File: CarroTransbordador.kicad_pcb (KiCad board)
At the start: 2 copper layers, 172.4 x 87.6 mm, 36 parts, among them J10 VIN- Pin, J11 VOUT+ Pin, J12 VOUT- Pin, J13 Borner ESP32, J14 Conn. Conv. HV, J15 Conn. Conv. LV, J16 Conn. ESP32, J17 Conn. LED Tr., J18 Conn. LED Empot., J19 Conn. LED Polea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

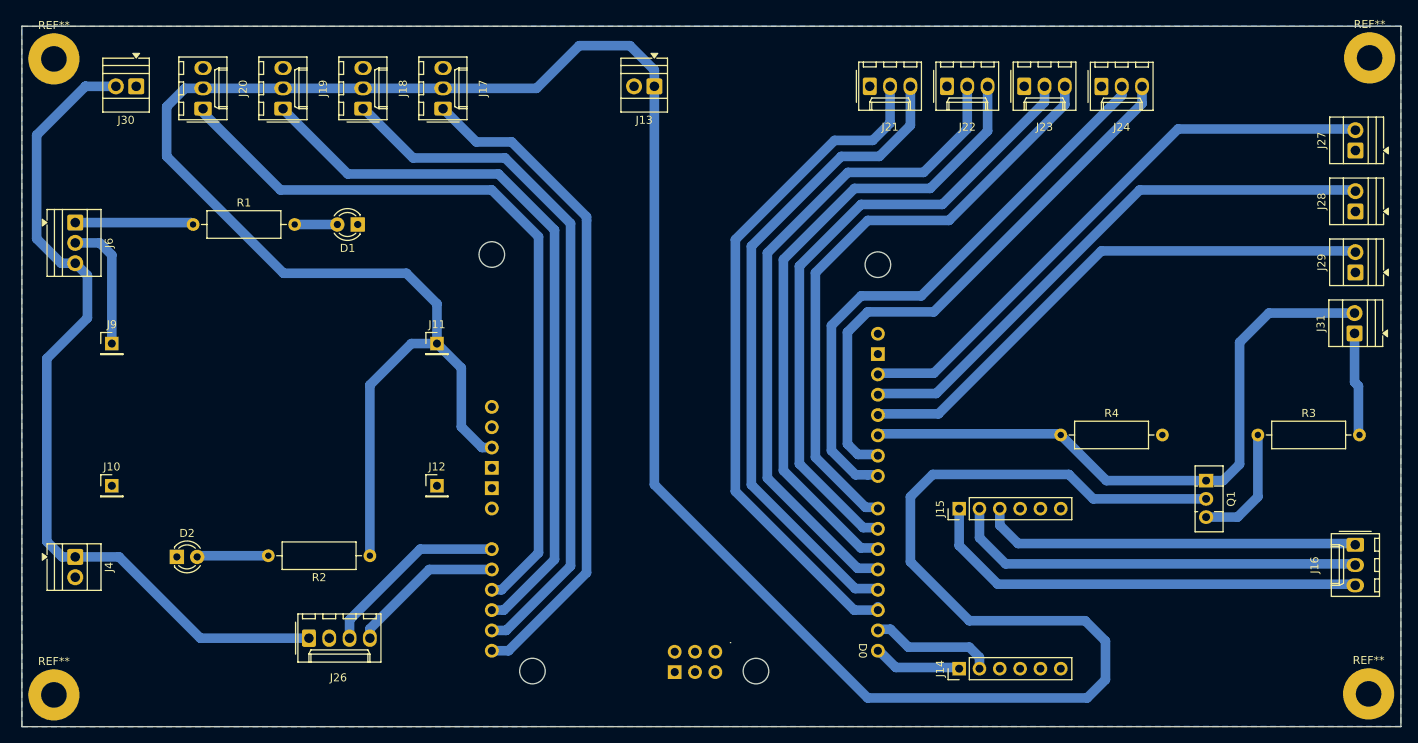
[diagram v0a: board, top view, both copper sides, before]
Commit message: Version mandada para PCB
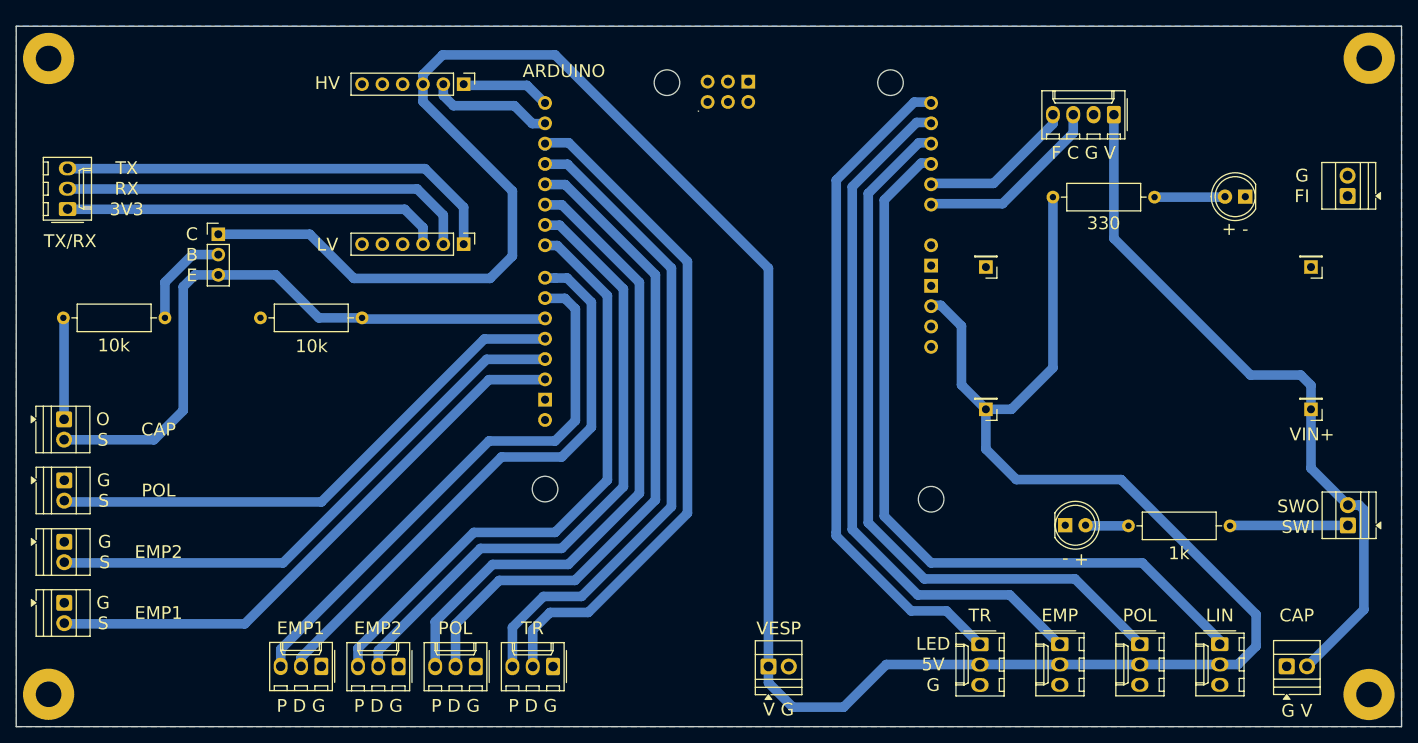
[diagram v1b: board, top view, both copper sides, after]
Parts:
- removed J6: Screw_Terminal_01x03, TerminalBlock:TerminalBlock_Xinya_XY308-2.54-3P_1x03_P2.54mm_Horizontal
- removed Q1: 2N222, Package_TO_SOT_THT:TO-126-3_Vertical
- added J40: Borner Switch IN, TerminalBlock:TerminalBlock_Xinya_XY308-2.54-2P_1x02_P2.54mm_Horizontal, F.Cu at (188.9, 81.6)
- added J8: Conn. BJT, Connector_PinHeader_2.54mm:PinHeader_1x03_P2.54mm_Vertical, F.Cu at (47.7, 45.2)
- D1, D2: footprint LED_THT:LED_D3.0mm -> LED_THT:LED_D5.0mm
- moved REF** 183.3 mm to (26.5, 102.7), turned to 180 degrees
- moved REF** 183.1 mm to (26.5, 23.2), turned to 180 degrees
- moved REF** 182.7 mm to (191.6, 23.2), turned to 180 degrees
- moved REF** 182.6 mm to (191.6, 102.7), turned to 180 degrees
- moved J27 171.0 mm to (28.5, 91.2), turned to -90 degrees
- moved J28 166.6 mm to (28.5, 83.6), turned to -90 degrees
- moved J16 166.3 mm to (28.9, 42.0), turned to 90 degrees
- moved J4 165.3 mm to (188.9, 40.4), turned to 90 degrees
- moved J29 163.5 mm to (28.5, 75.9), turned to -90 degrees
- moved J31 161.7 mm to (28.4, 68.3), turned to -90 degrees
- moved J30 161.1 mm to (181.3, 99.2), turned to 0 degrees
- moved J10 152.4 mm to (184.3, 49.3), turned to 180 degrees
- moved J9 150.1 mm to (184.3, 67.0), turned to 180 degrees
- moved J20 143.6 mm to (172.9, 96.4), turned to -90 degrees
- moved D2 140.9 mm to (176.1, 40.5), turned to 180 degrees
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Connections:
- J14 pad 3: /ModuloControladores/5V_ARDUINO -> +5V
- J4 pad 1: /ModuloActuadores/PWR_LINEAR -> /ModuloEnergia/F6A_IN
- J9 pad 1: /ModuloEnergia/REG_IN+ -> /ModuloActuadores/PWR_LINEAR
- R3 pad 1: Net-(Q1-B) -> /ModuloSensores/BASE_BJT
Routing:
- net +5V: track 367.4 -> 339.7 mm
- net /ModuloActuadores/PWR_LINEAR: track 106.8 -> 89.4 mm
- net /ModuloEnergia/REG_IN+: track 16.3 -> 0.00 mm
- net Net-(Q1-B): track 15.2 -> 0.00 mm
- net /ModuloSensores/BASE_BJT: track 0.00 -> 12.5 mm
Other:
- board size 172.4 x 87.6 mm -> 173.2 x 87.6 mm
- board text added: "+ -"
- board text added: "ARDUINO"
- board text added: "C B E"
- board text added: "CAP"
- board text added: "EMP"
- board text added: "EMP1"
- board text added: "EMP2"
- board text added: "ESP32"
- board text added: "F C G V"
- board text added: "G FI"
- board text added: "G S"
- board text added: "G V"
- board text added: "HV"
- board text added: "LED 5V G"
- board text added: "LIN"
- board text added: "LV"
- board text added: "O S"
- board text added: "P D G"
- board text added: "POL"
- board text added: "SWO SWI"
- board text added: "TR"
- board text added: "TX RX 3V3"
- board text added: "TX/RX"
- board text added: "V G"
- board text added: "VESP"
- board text added: "VIN+"
